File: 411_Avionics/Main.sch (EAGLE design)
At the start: 10 parts, among them IC1 BQ24022, U2 ATTINY85V-10SU, U3 LSM9DS0, U4 74HC151D

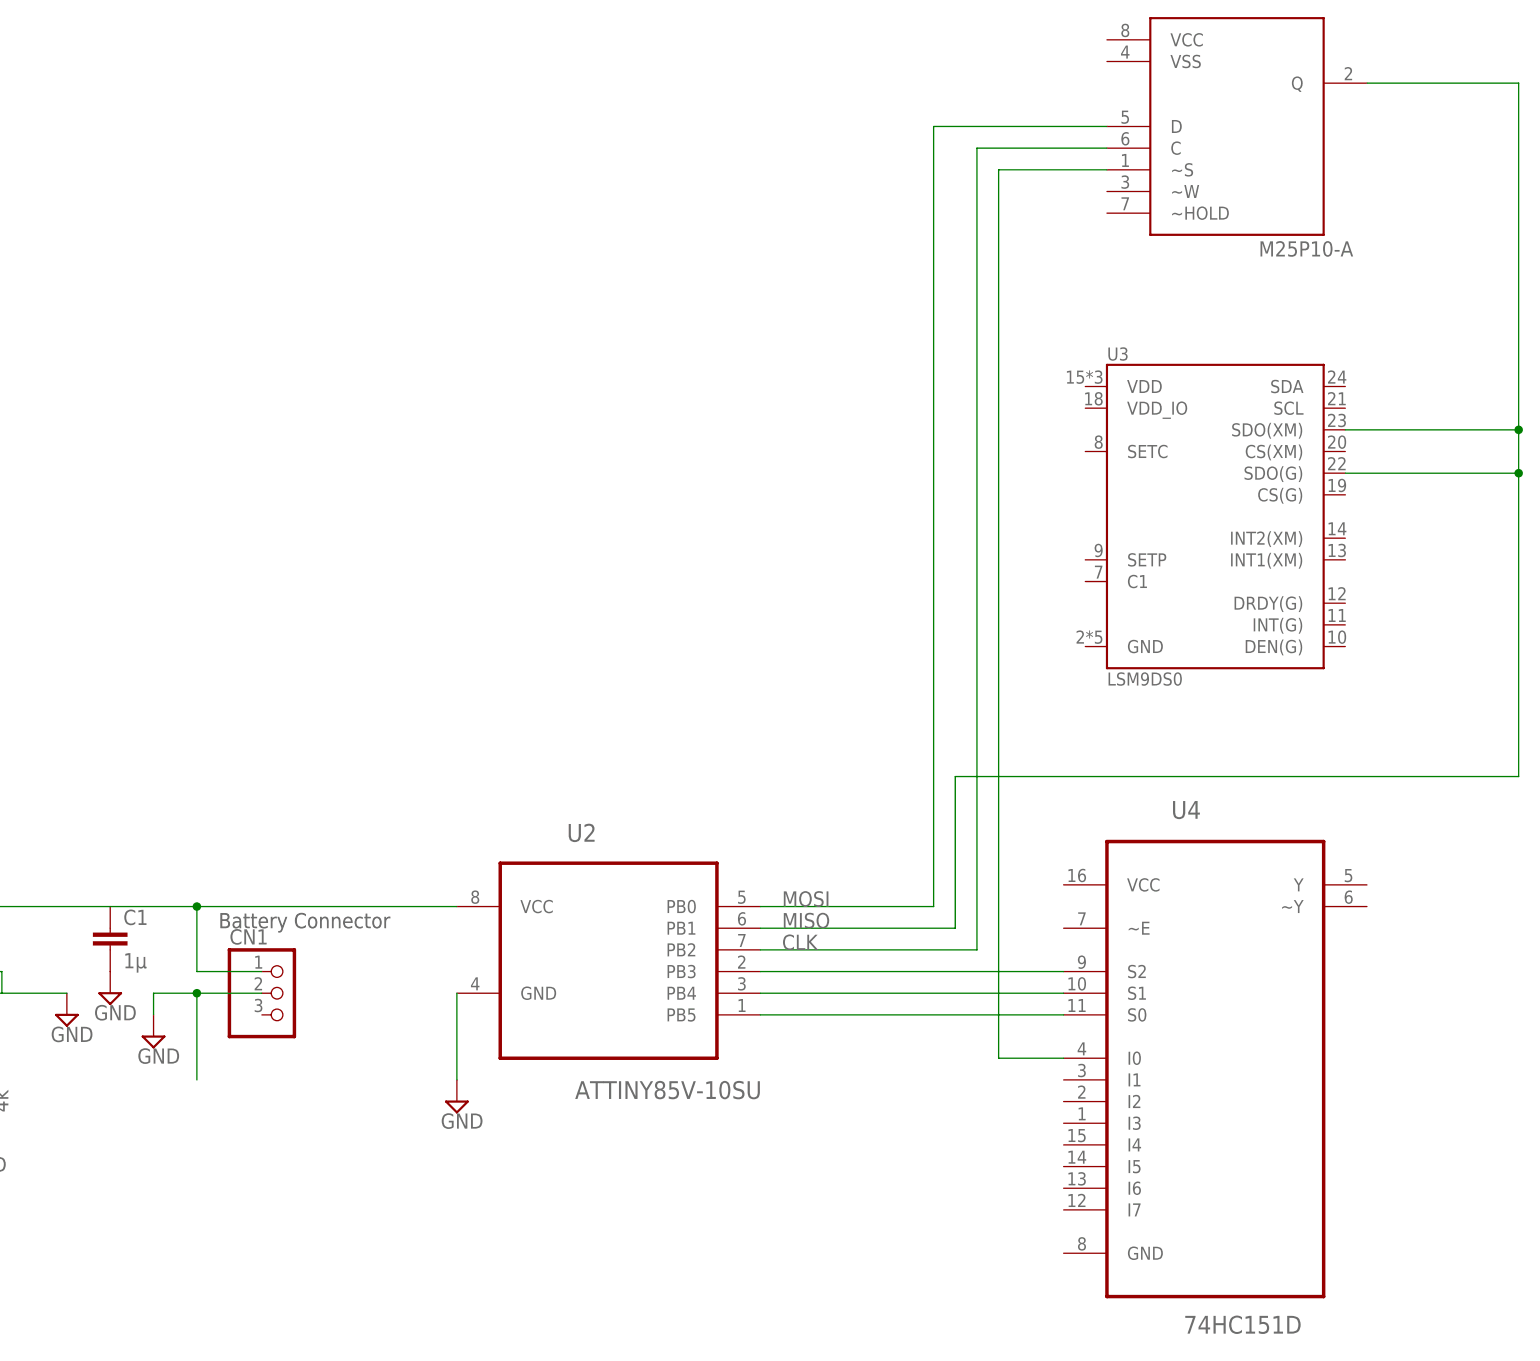
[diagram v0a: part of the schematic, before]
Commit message: Updated sensor connections on schematic.
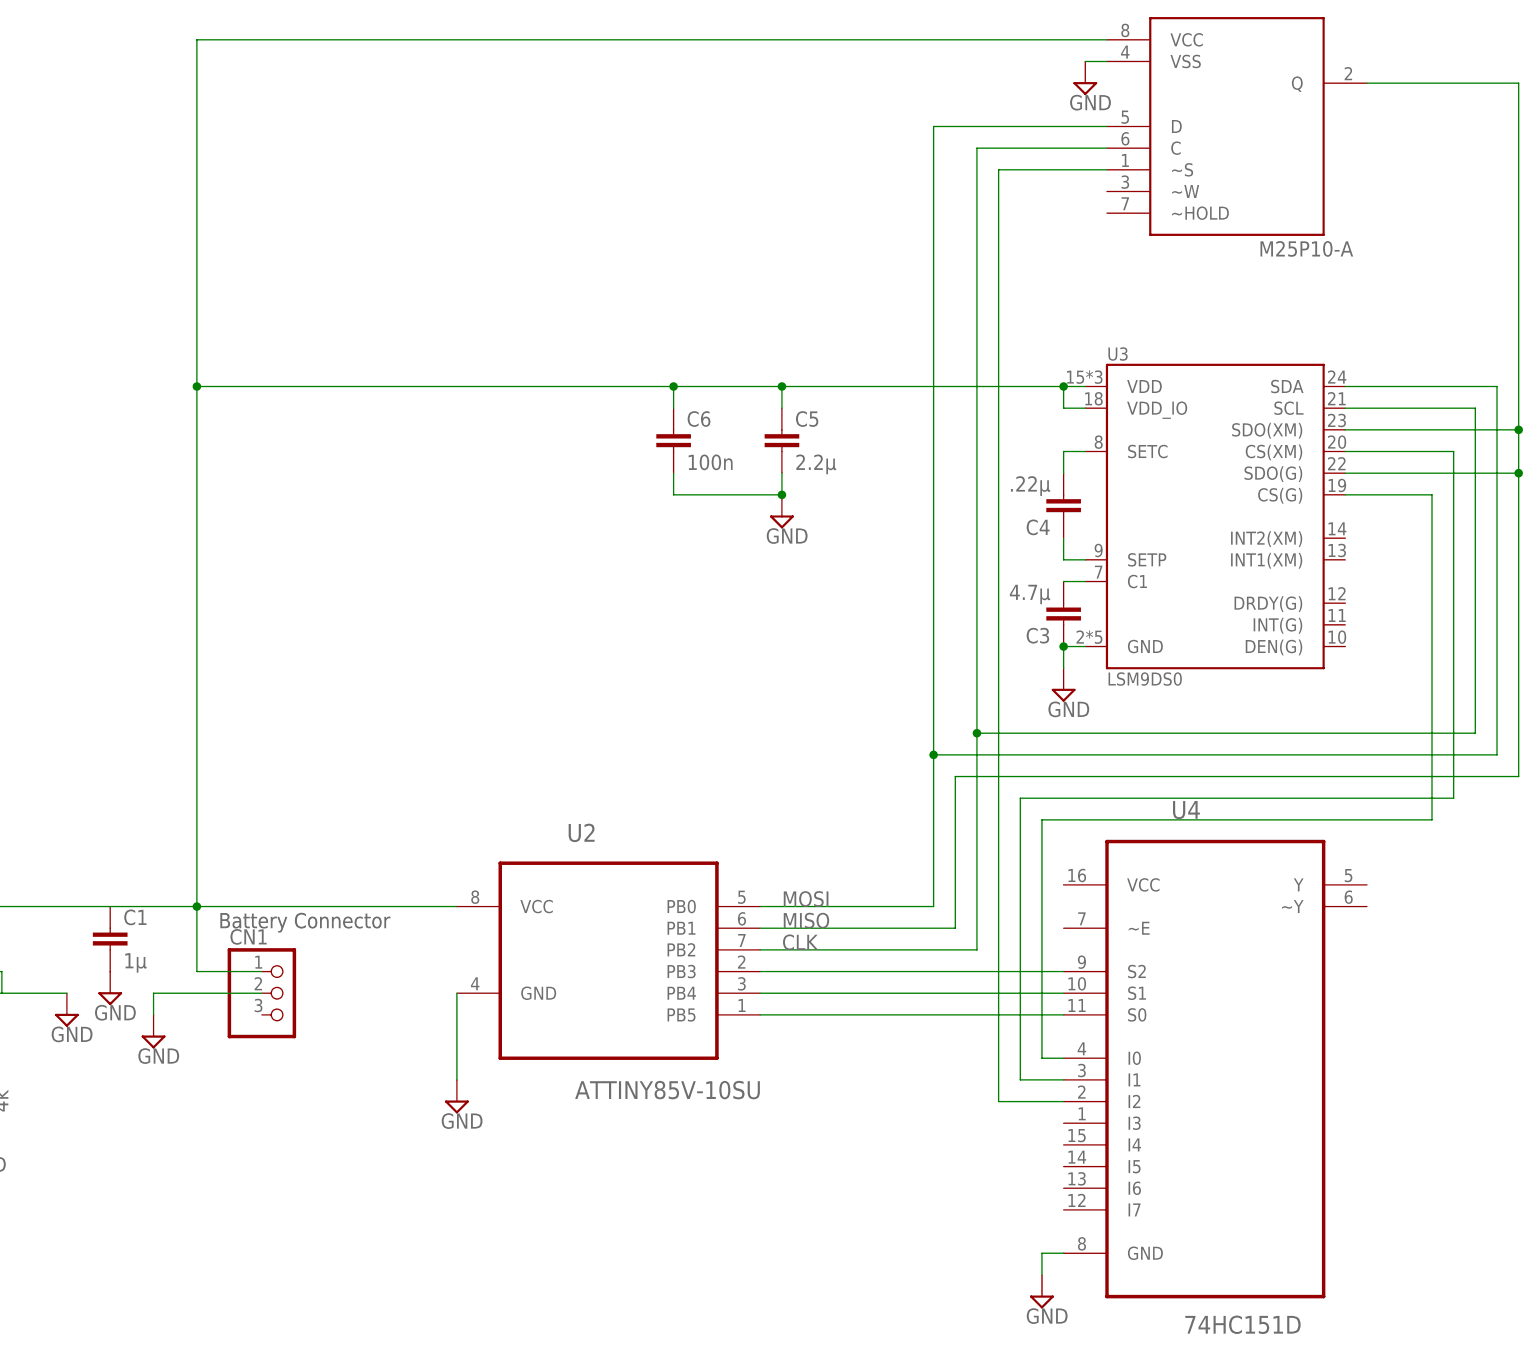
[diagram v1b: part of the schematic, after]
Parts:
- added C3: 4.7µ, rcl:C-EUC0805
- added C4: .22µ, rcl:C-EUC0805
- added C5: 2.2µ, rcl:C-EUC0805
- added C6: 100n, rcl:C-EUC0805
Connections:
- new net N$10: C4.2, U3.SETC
- new net N$11: C4.1, U3.SETP
- new net N$8: U3.CS(XM), U4.I1
- new net N$9: C3.2, U3.C1
- new net VCC: C1.1, C5.1, C6.1, CN1.1, IC1G$1.OUT, U$1.VCC, U2.VCC, U3.VDD, U3.VDD_IO
- net CLK: now also U3.SCL
- net GND: now also C3.1, C5.2, C6.2, U$1.VSS, U3.GND, U4.GND
- net MEM: now also U4.I2; no longer U4.I0
- net MOSI: now also U3.SDA
- net N$5: now also U3.CS(G), U4.I0; no longer C1.1, CN1.1, IC1G$1.OUT, U2.VCC

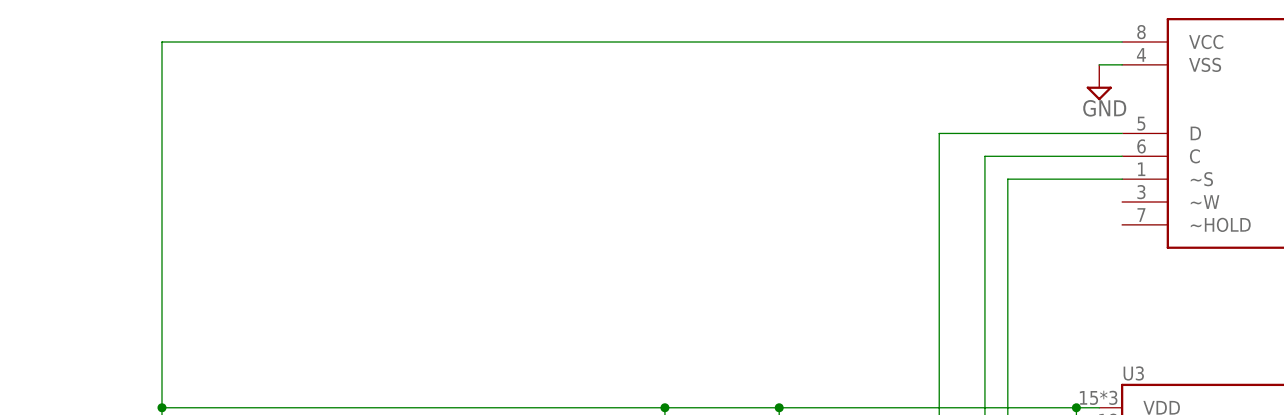
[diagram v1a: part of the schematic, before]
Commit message: Lifted flash memory unused pins in schematic
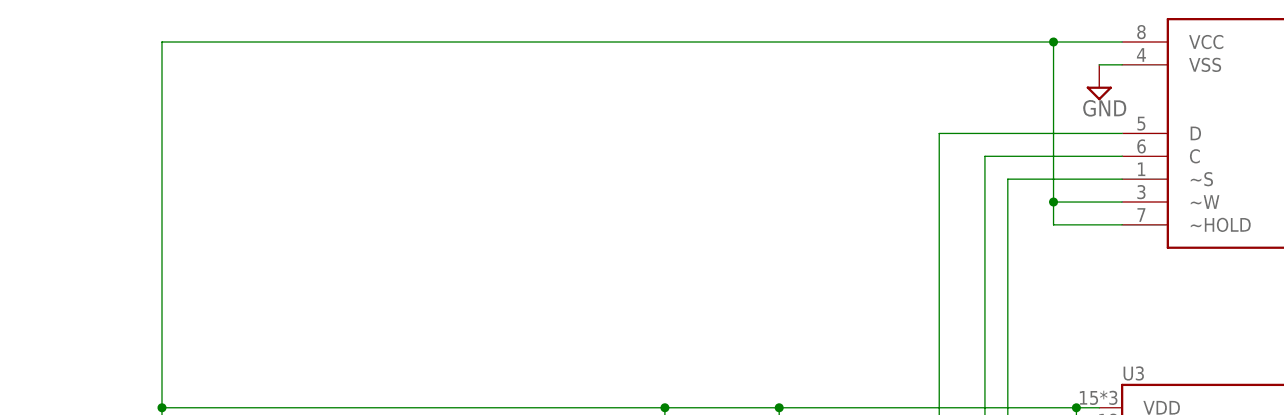
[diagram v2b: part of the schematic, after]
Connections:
- net VCC: now also U$1.~HOLD, U$1.~W
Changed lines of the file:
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@@
 <?xml version="1.0" encoding="utf-8"?>
 <!DOCTYPE eagle SYSTEM "eagle.dtd">
-<eagle version="7.5.0">
+<eagle version="7.7.0">
 <drawing>
 <settings>
@@
 <wire x1="-20.32" y1="76.2" x2="-20.32" y2="15.24" width="0.1524" layer="91"/>
 <pinref part="U$1" gate="G$1" pin="VCC"/>
-<wire x1="86.36" y1="116.84" x2="-20.32" y2="116.84" width="0.1524" layer="91"/>
+<wire x1="86.36" y1="116.84" x2="78.74" y2="116.84" width="0.1524" layer="91"/>
+<wire x1="78.74" y1="116.84" x2="-20.32" y2="116.84" width="0.1524" layer="91"/>
 <wire x1="-20.32" y1="116.84" x2="-20.32" y2="76.2" width="0.1524" layer="91"/>
 <junction x="-20.32" y="76.2"/>
-</segment>
-</net>
+<pinref part="U$1" gate="G$1" pin="~HOLD"/>
+<wire x1="86.36" y1="96.52" x2="78.74" y2="96.52" width="0.1524" layer="91"/>
+<wire x1="78.74" y1="96.52" x2="78.74" y2="99.06" width="0.1524" layer="91"/>
+<junction x="78.74" y="116.84"/>
+<pinref part="U$1" gate="G$1" pin="~W"/>
+<wire x1="78.74" y1="99.06" x2="78.74" y2="116.84" width="0.1524" layer="91"/>
+<wire x1="86.36" y1="99.06" x2="78.74" y2="99.06" width="0.1524" layer="91"/>
+<junction x="78.74" y="99.06"/>
+</segment>
+</net>

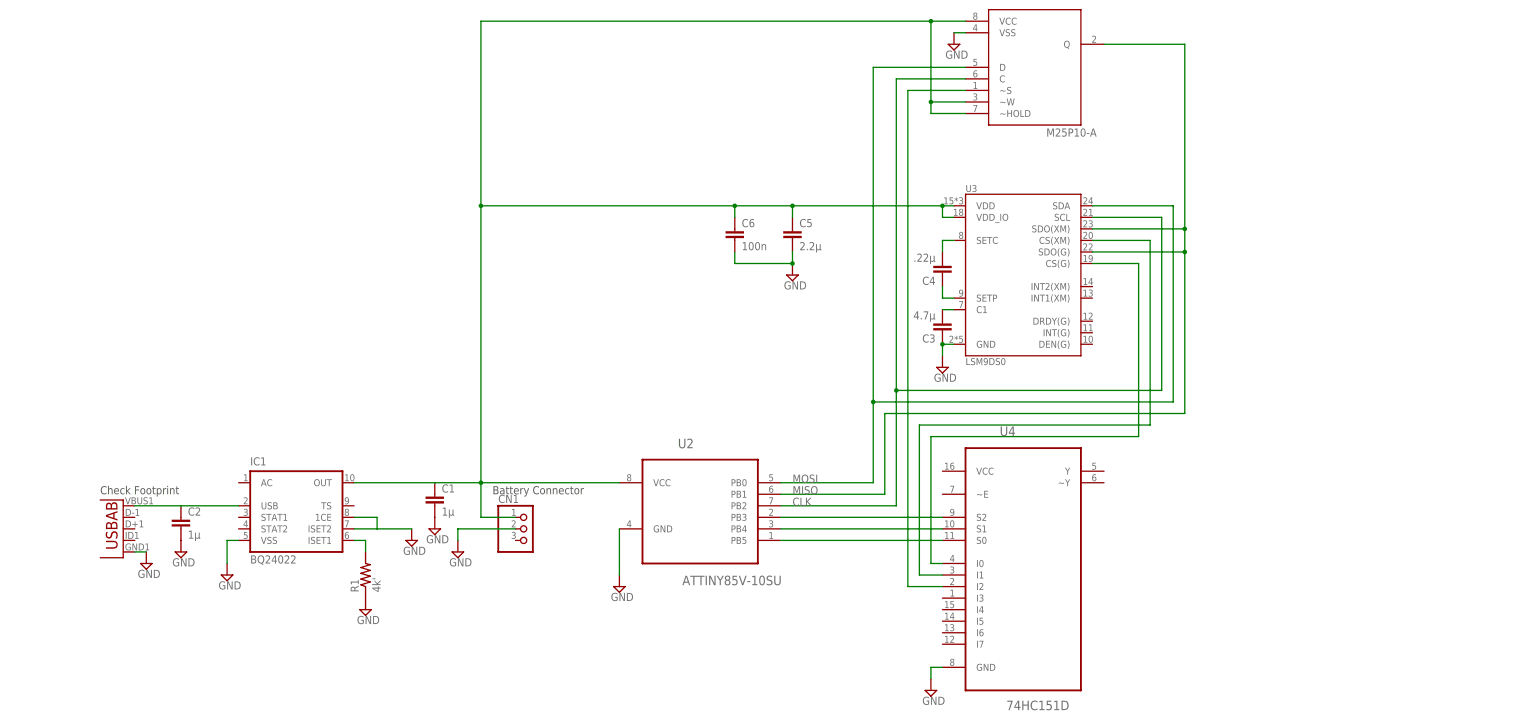
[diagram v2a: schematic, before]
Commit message: Almost finished schematic, left to be done:
-Connect MUX to proper pins
-Processor Interfacing
-Still need to change USB connection
-Finish footprints
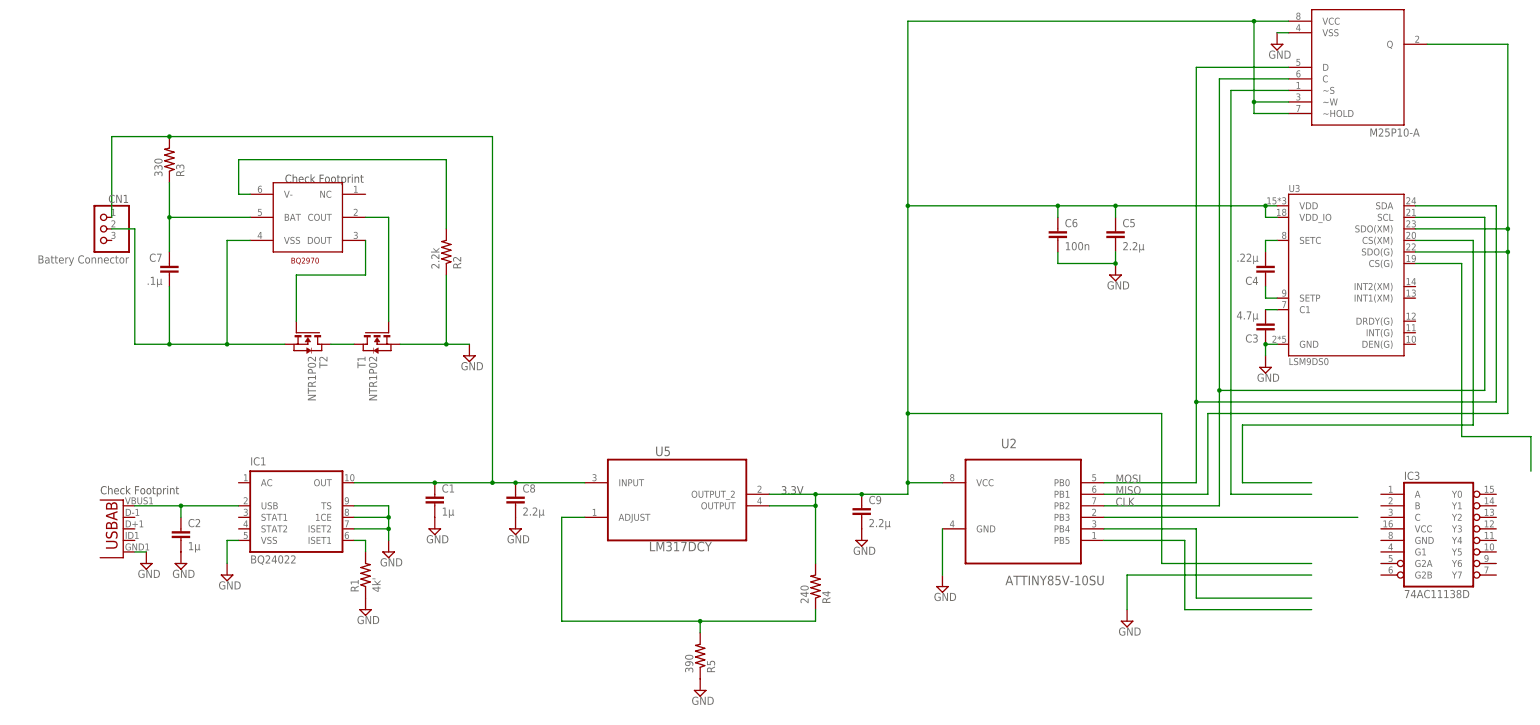
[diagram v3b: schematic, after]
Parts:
- removed U4: 74HC151D, 74HC151D:74HC151D
- added C7: .1µ, rcl:C-EUC0805
- added C8, C9: 2.2µ, rcl:C-EU050-025X075
- added IC3: 74AC11138D, 74ac-logic:74AC11138D
- added R2: 2.2k, resistor:R-US_R0805
- added R3: 330, resistor:R-US_R0805
- added R4: 240, resistor:R-US_R0805
- added R5: 390, resistor:R-US_R0805
- added T1, T2: NTR1P02, zetex:NMOSSOT23
- added U$2: BQ2970, WSON-6-PAD:BQ2970
- added U5: LM317DCY, LM317DCY:LM317DCY
- CN1: value (none) -> Battery Connector
- U1: value (none) -> USB_In
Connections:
- removed net N$2: C2.1, IC1G$1.USB
- new net N$12: T1.G, U$2.COUT
- new net N$13: T2.G, U$2.DOUT
- new net N$14: T1.D, T2.D
- new net N$15: C7.1, R3.1, U$2.BAT
- new net N$16: C7.2, CN1.2, T2.S, U$2.VSS
- new net N$17: R2.2, U$2.V-
- new net N$18: C1.1, C8.1, CN1.1, IC1G$1.OUT, R3.2, U5.INPUT
- new net N$20: R4.1, R5.2, U5.ADJUST
- net GND: now also C8.2, C9.2, IC1G$1.TS, R2.1, R5.1, T1.S; no longer CN1.2, U4.GND
- net MEM: no longer U4.I2
- net N$1: now also C2.1, IC1G$1.USB
- net N$3: no longer U4.S2
- net N$5: no longer U4.I0
- net N$6: no longer U4.S1
- net N$7: no longer U4.S0
- net N$8: no longer U4.I1
- net VCC: now also C9.1, R4.2, U5.OUTPUT, U5.OUTPUT_2; no longer C1.1, CN1.1, IC1G$1.OUT
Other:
- note added: "3.3V"
- note removed: "Battery Connector"
- moved on the sheet: C2, C3, C4, C5, C6, CN1, U2, U3

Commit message: Schematic reorganized and touched up
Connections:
- removed net MEM: U$1.~S
- removed net N$3: U2.PB3
- removed net N$5: U3.CS(G)
- removed net N$6: U2.PB4
- removed net N$7: U2.PB5
- removed net N$8: U3.CS(XM)
- new net GYR_EN: IC3.Y1, U3.CS(G)
- new net MEM_EN: IC3.Y0, U$1.~S
- new net SEL0: IC3.A, U2.PB3
- new net SEL1: IC3.B, U2.PB4
- new net SEL2: IC3.C, U2.PB5
- new net XM_EN: IC3.Y2, U3.CS(XM)
- net GND: now also C9.1, IC3.G2A, IC3.G2B, IC3.GND; no longer C9.2
- net N$17: now also C1.1, C8.1, IC1G$1.OUT, U5.INPUT
- net N$18: no longer C1.1, C8.1, IC1G$1.OUT, U5.INPUT
- net VCC: now also C9.2, IC3.G1, IC3.VCC; no longer C9.1
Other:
- note added: "00000001"
- note added: "A"
- note added: "Demultiplexer"
- note added: "Flash Memory"
- note added: "Microcontroller"
- note added: "Model Rocket Avionics Schematic Diagram"
- note added: "Power Supply"
- note added: "Sensors"
- note removed: "3.3V"
- moved on the sheet: C1, C2, C3, C4, C5, C6, C7, C8, C9, CN1, IC1, IC3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

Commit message: Minor changes to schematic power logic.  Also added a couple bypass capacitors to output of LM317.
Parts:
- added C10: 100n, rcl:C-EUC0805
- C8: value 2.2µ -> .1µ
- C9: device rcl:C-EU050-025X075 -> rcl:C-EUC0805
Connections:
- new net N$3: U$1.VCC, U$1.~HOLD, U$1.~W
- new net N$5: C5.1, C6.1, U3.VDD, U3.VDD_IO
- net GND: now also C10.2, C9.2; no longer C9.1
- net VCC: now also C10.1, C9.1; no longer C5.1, C6.1, C9.2, U$1.VCC, U$1.~HOLD, U$1.~W, U3.VDD, U3.VDD_IO
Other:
- note added: "All capacitors 16 V rating, XR7 All resistors 1W rating, 1%"
- note added: "Model Rocket Avionics, Team 11 Schematic Diagram"
- note removed: "Model Rocket Avionics Schematic Diagram"
- moved on the sheet: C9
